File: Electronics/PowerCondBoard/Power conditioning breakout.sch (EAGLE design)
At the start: 45 parts

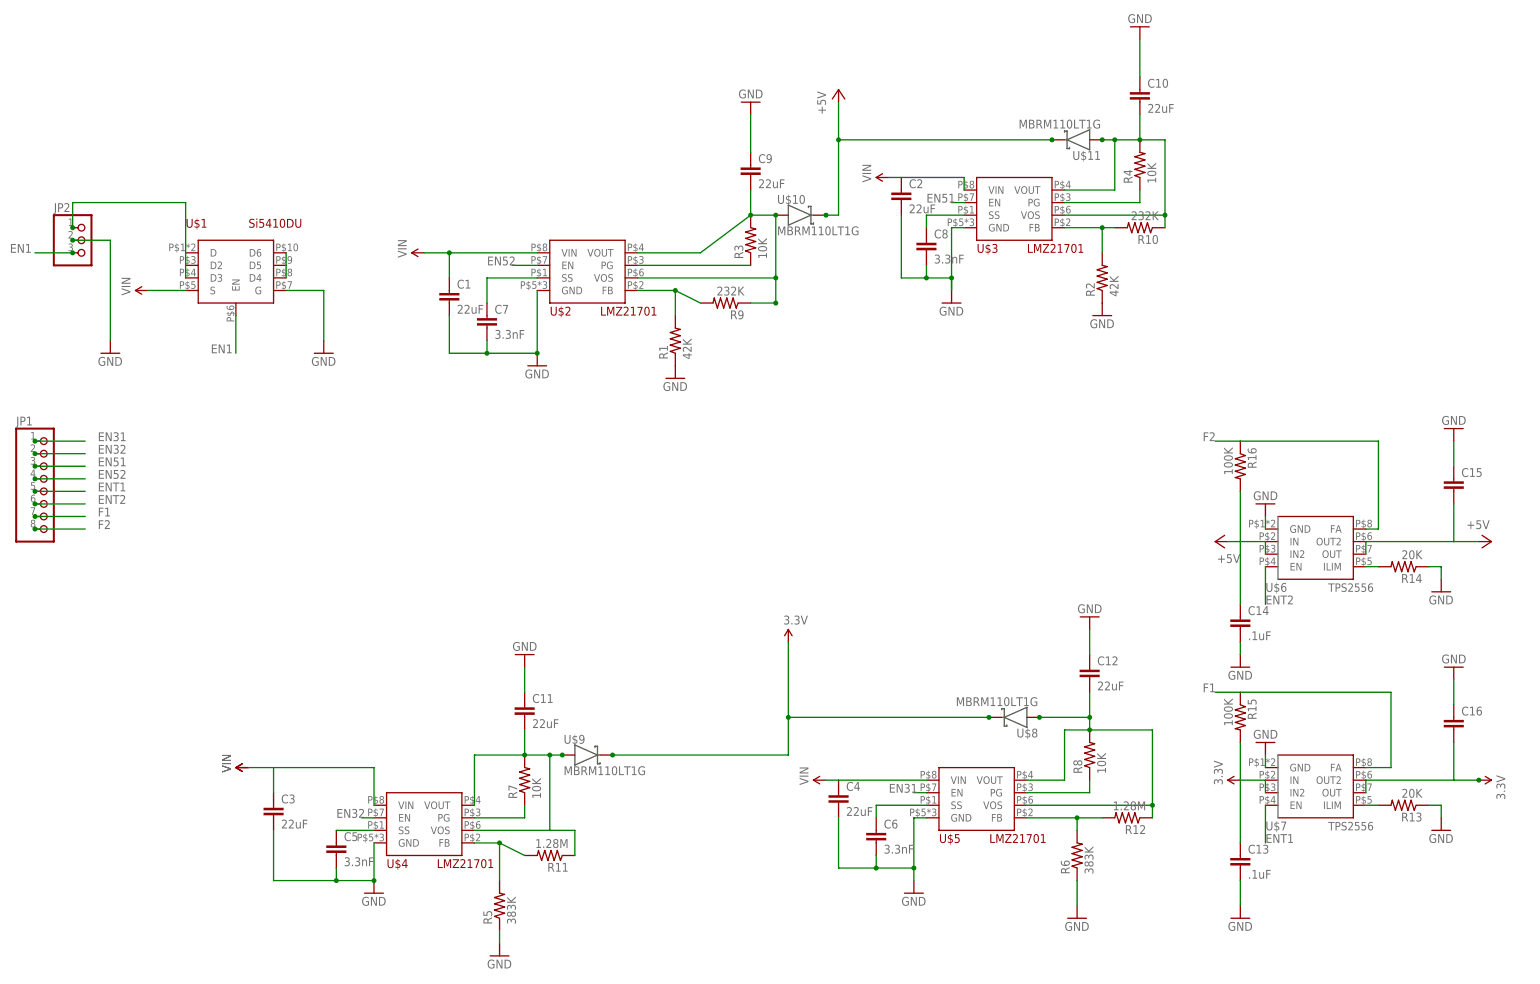
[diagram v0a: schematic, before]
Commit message: Power Cond Board
put in break points, changed the diodes and fixed resistor values
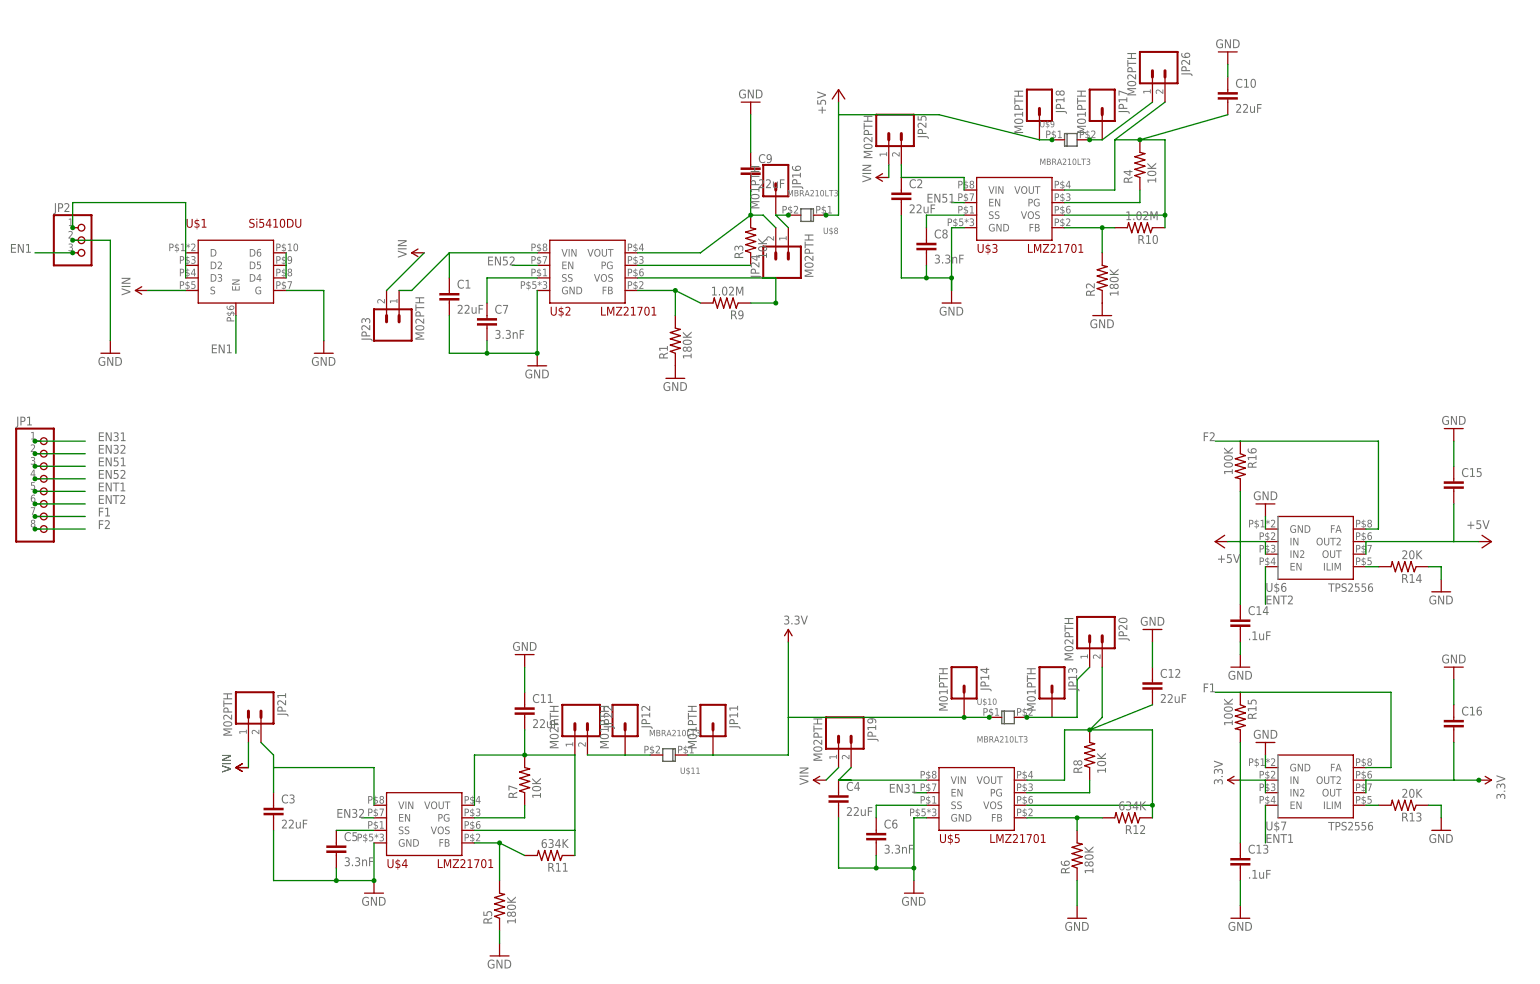
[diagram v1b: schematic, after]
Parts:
- added JP11, JP12, JP13, JP14, JP16, JP17, JP18: M01PTH, SparkFun-Connectors:M01PTH
- added JP19, JP20, JP21, JP22, JP23, JP24, JP25, JP26: M02PTH, SparkFun-Connectors:M02PTH
- R1, R2: value 42K -> 180K
- R10, R9: value 232K -> 1.02M
- R11, R12: value 1.28M -> 634K
- R5, R6: value 383K -> 180K
- U$10, U$11, U$8, U$9: value MBRM110LT1G -> MBRA210LT3; device RitLaunchInitiative:MBRM110LT1G -> RitLaunchInitiative:MBRA210LT3
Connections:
- new net N$14: C9.2, JP24.2, R3.2, U$2.VOUT
- new net N$18: C11.2, JP22.1, R11.1, R7.2, U$4.VOS, U$4.VOUT
- new net N$20: C3.1, JP21.2, U$4.VIN
- new net N$24: C4.1, JP19.2, U$5.VIN
- new net N$25: JP13.1, JP20.1, U$10.P$2
- new net N$26: JP16.1, JP24.1, U$8.P$2
- new net N$27: JP17.1, JP26.1, U$9.P$2
- new net N$28: C1.1, JP23.1, U$2.VIN
- new net N$29: C2.1, JP25.2, U$3.VIN
- net +5V: now also JP18.1, U$8.P$1, U$9.P$1
- net 3.3V: now also JP11.1, JP14.1, U$10.P$1, U$11.P$1; no longer U$8.P$2
- net N$1: no longer C9.2, R3.2, U$10.P$1, U$2.VOUT
- net N$10: now also JP12.1, JP22.2, U$11.P$2; no longer C11.2, R11.1, R7.2, U$4.VOS, U$4.VOUT, U$9.P$1
- net N$21: now also JP20.2; no longer U$8.P$1
- net N$5: now also JP26.2; no longer U$11.P$1
- net VIN: now also JP19.1, JP21.1, JP23.2, JP25.1; no longer C1.1, C2.1, C3.1, C4.1, U$2.VIN, U$3.VIN, U$4.VIN, U$5.VIN
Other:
- moved on the sheet: C10, C12

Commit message: Power Board changes
more organized sch, and the MBRA210LT3 has had its symbol changed to its
appropriate symbol
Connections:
- removed net N$1 (its old number): R9.1, U$2.VOS
- removed net N$14: C9.2, JP24.2, R3.2, U$2.VOUT
- new net N$31: C9.2, JP24.2, R3.2, R9.1, U$2.VOS, U$2.VOUT
- net +5V: now also U$10.P$1, U$11.P$1; no longer U$8.P$1, U$9.P$1
- net 3.3V: now also U$8.P$1, U$9.P$1; no longer U$10.P$1, U$11.P$1
- net N$10: now also U$9.P$2; no longer U$11.P$2
- net N$20: now also JP21.1; no longer JP21.2
- net N$24: now also JP19.1; no longer JP19.2
- net N$25: now also U$8.P$2; no longer U$10.P$2
- net N$26: now also U$10.P$2; no longer U$8.P$2
- net N$27: now also U$11.P$2; no longer U$9.P$2
- net VIN: now also JP19.2, JP21.2; no longer JP19.1, JP21.1
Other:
- moved on the sheet: C10, C11, C12, C2, C3, C4, C6, C8, C9, JP16, JP17, JP18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

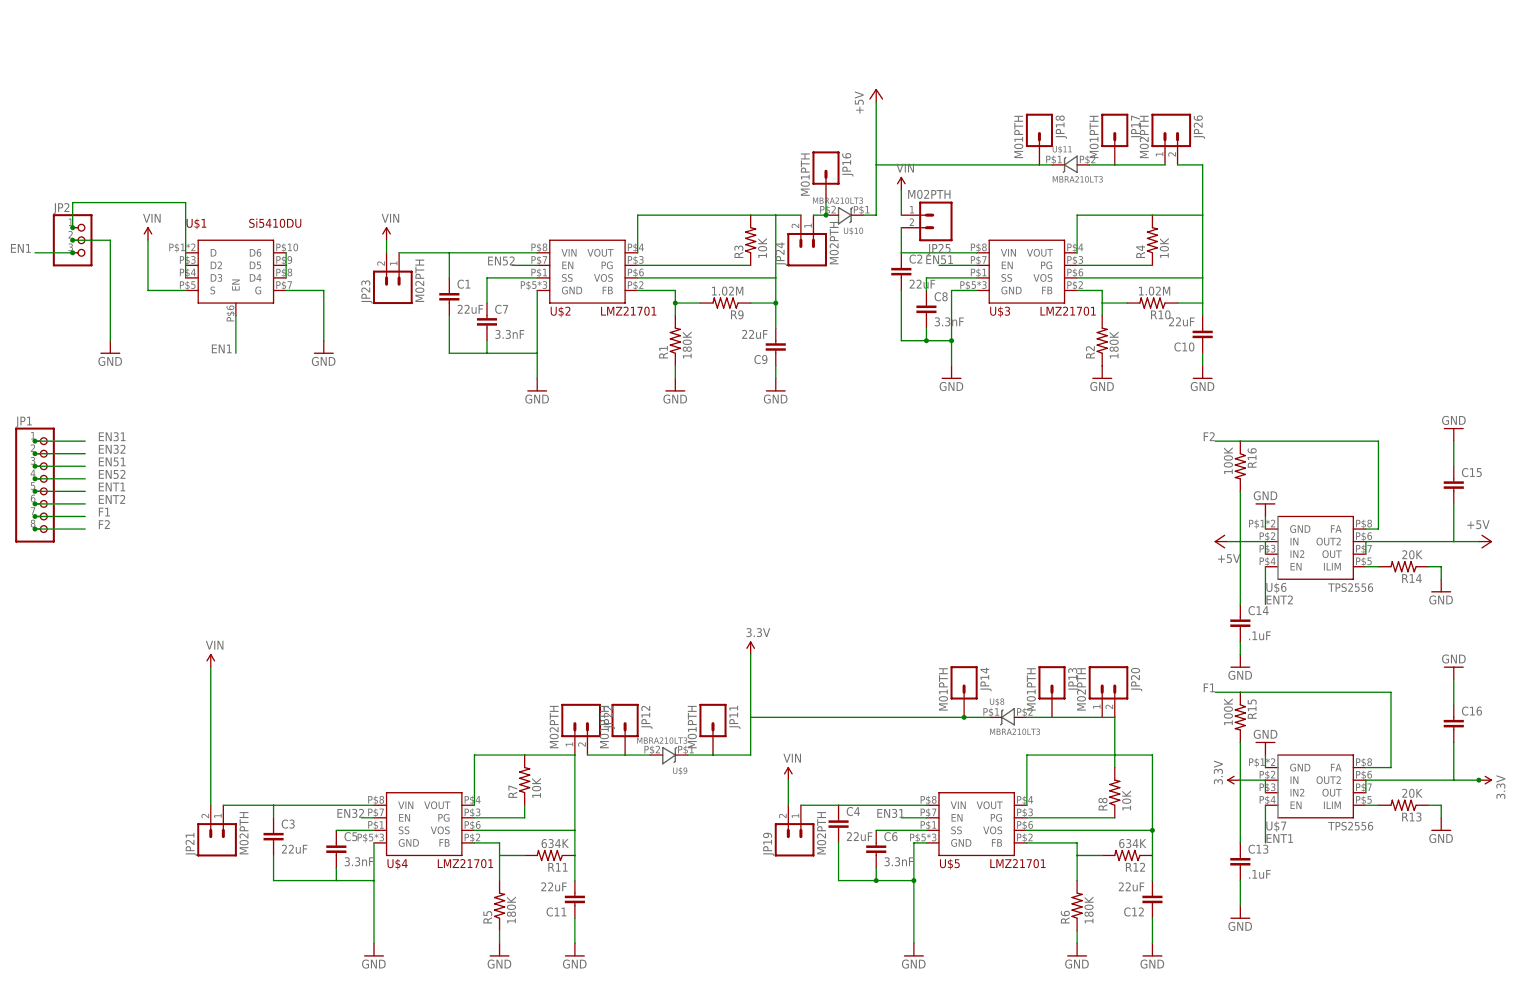
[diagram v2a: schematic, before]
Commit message: Power Cond PCB
ready for review
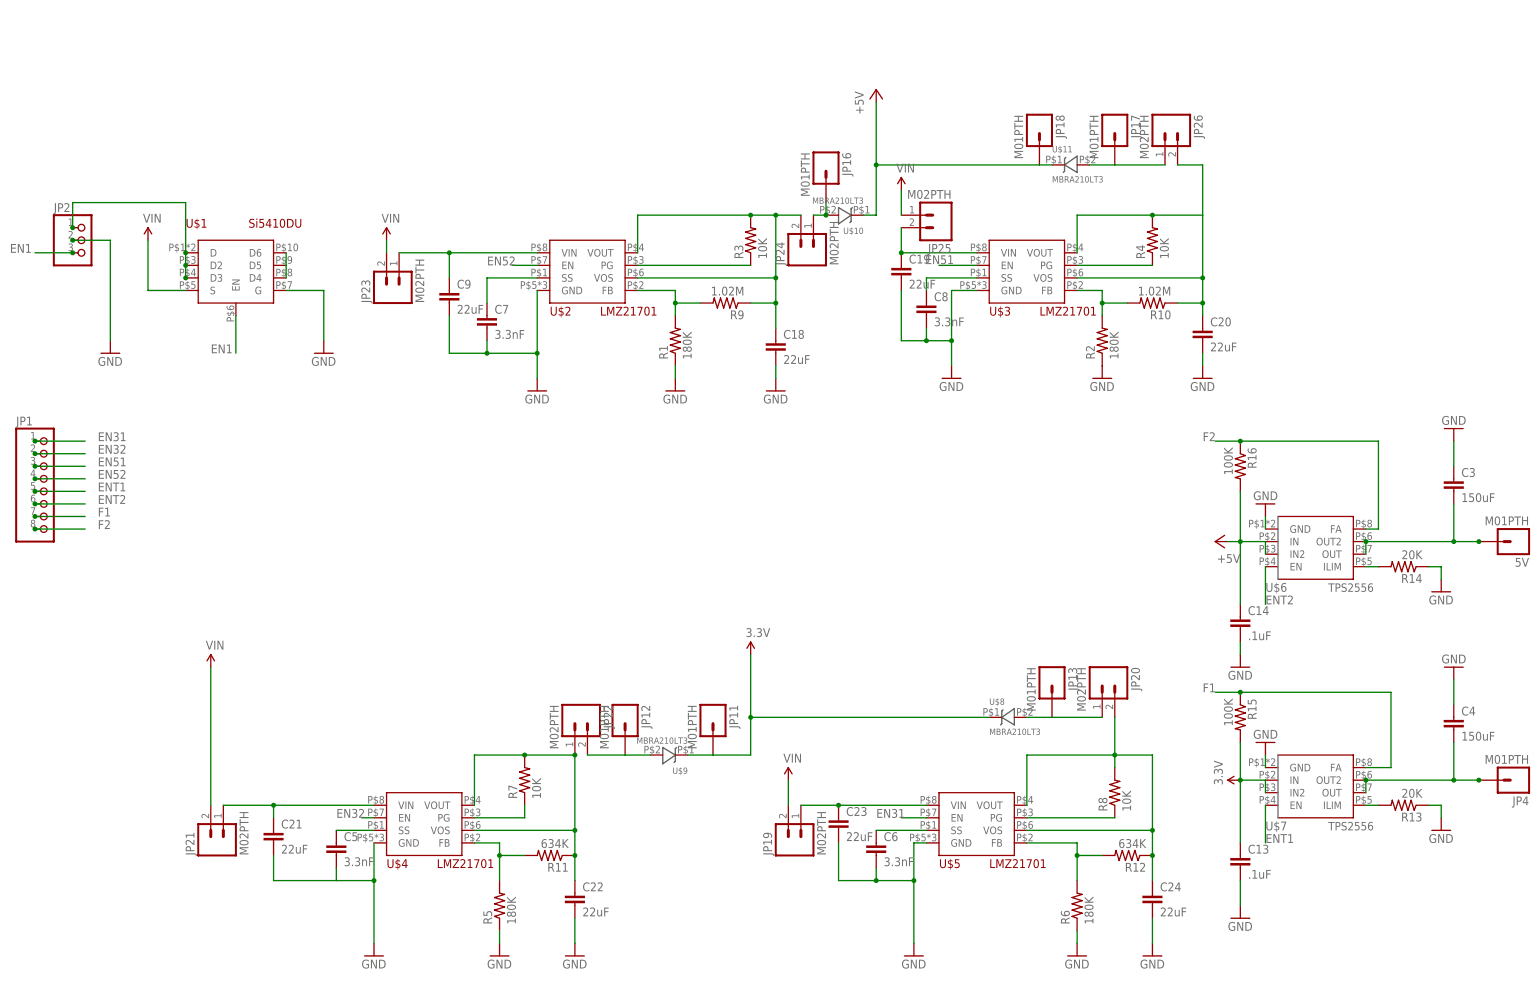
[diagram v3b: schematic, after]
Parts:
- removed C1, C2: 22uF, SparkFun-Capacitors:22UF-16V-20%-(1210)
- removed C10, C11, C12: 22uF, SparkFun-Capacitors:22UF-6.3V-20%(0805)
- removed C15, C16: (no value), SparkFun-Passives:CAP0603-CAP
- removed JP14: M01PTH, SparkFun-Connectors:M01PTH
- added 5V, JP4: M01PTH, SparkFun-Connectors:M01PTH
- added C18, C19, C20, C21, C22, C23, C24: 22uF, SparkFun-Capacitors:22UF-6.3V-20%(0805)
- C3, C4: value 22uF -> 150uF; device SparkFun-Capacitors:22UF-16V-20%-(1210) -> SparkFun-Capacitors:100UF6.3V20%(1210)
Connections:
- new net N$14: 5V.1, C3.2, U$6.OUT, U$6.OUT2
- new net N$5: C4.2, JP4.1, U$7.OUT, U$7.OUT2
- net +5V: no longer C15.2, U$6.OUT, U$6.OUT2
- net 3.3V: no longer C16.2, JP14.1, U$7.OUT, U$7.OUT2
- net GND: now also C18.2, C19.2, C20.2, C21.2, C22.2, C23.2, C24.2, C3.1, C4.1, C9.2; no longer C1.2, C10.1, C11.1, C12.1, C15.1, C16.1, C2.2, C3.2, C4.2, C9.1
- net N$1: now also C20.1; no longer C10.2
- net N$18: now also C22.1; no longer C11.2
- net N$20: now also C21.1; no longer C3.1
- net N$21: now also C24.1; no longer C12.2
- net N$24: now also C23.1; no longer C4.1
- net N$28: now also C9.1; no longer C1.1
- net N$29: now also C19.1; no longer C2.1
- net N$31: now also C18.1; no longer C9.2
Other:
- moved on the sheet: C3, C4, C9
